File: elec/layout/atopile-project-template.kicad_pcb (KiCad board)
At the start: 2 copper layers, 40 x 40 mm, 2 parts

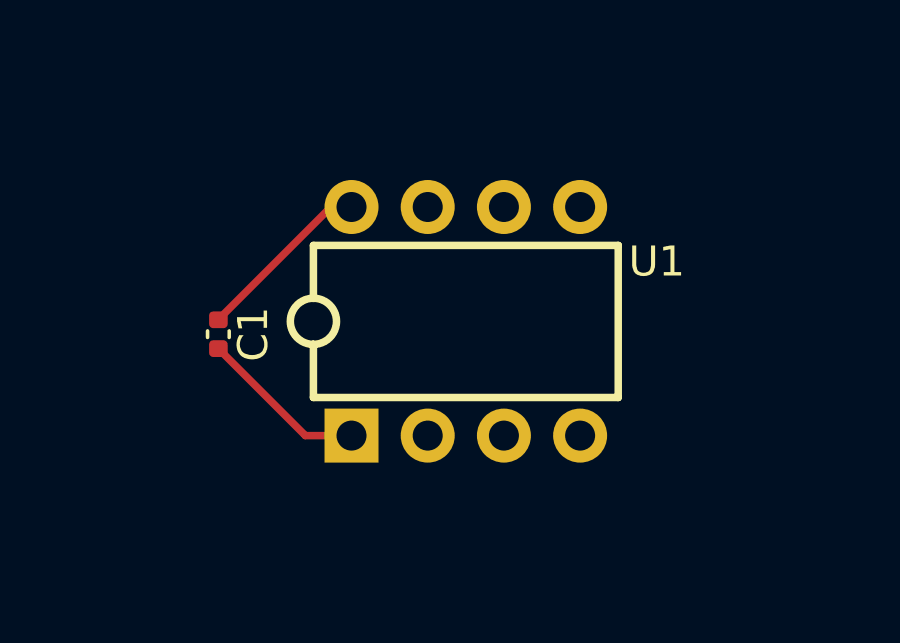
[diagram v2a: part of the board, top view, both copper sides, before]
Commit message: remove the old layout
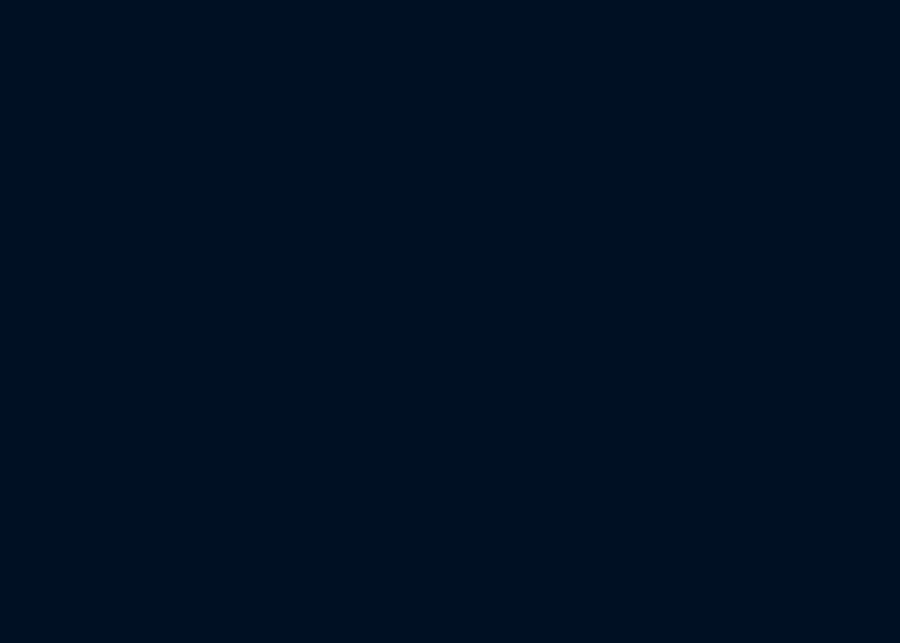
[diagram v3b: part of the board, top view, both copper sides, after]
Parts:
- removed C1: 100nF, Capacitor_SMD:C_0402_1005Metric
- removed U1: , lib:DIP-8_L9.7-W6.4-P2.54-LS7.6-BL
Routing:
- net HelloWorld-vcc_5v: track 6.00 -> 0.00 mm
- net HelloWorld-gnd: track 5.64 -> 0.00 mm
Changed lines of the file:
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@@
   )
   (net 0 "")
-  (net 1 "HelloWorld-vcc_5v")
-  (net 2 "HelloWorld-gnd")
-  (net 3 "timer-trigger")
-  (net 4 "timer-output")
-  (net 5 "timer-reset")
-  (net 6 "timer-ctrl_v")
-  (net 7 "timer-threshold")
-  (net 8 "timer-discharge")
-  (footprint "lib:DIP-8_L9.7-W6.4-P2.54-LS7.6-BL" (layer "F.Cu")
-    (at 142.24 93.98)
-    (attr smd)
-    (fp_text reference "U1" (at 6.363769 -1.989911) (layer "F.SilkS")
-        (effects (font (size 1 1) (thickness 0.15)))
-    )
-    (fp_text value "" (at 0 7.81) (layer "F.Fab")
-        (effects (font (size 1 1) (thickness 0.15)))
-    )
-    (fp_text user "${REFERENCE}" (at 0 0) (layer "F.Fab")
-        (effects (font (size 1 1) (thickness 0.15)))
-    )
-    (fp_line (start -5.08 -2.53) (end 5.08 -2.53)
-      (stroke (width 0.25) (type solid)) (layer "F.SilkS"))
-    (fp_line (start -5.08 -0.76) (end -5.08 -2.53)
-      (stroke (width 0.25) (type solid)) (layer "F.SilkS"))
-    (fp_line (start -5.08 2.54) (end -5.08 0.77)
-      (stroke (width 0.25) (type solid)) (layer "F.SilkS"))
-    (fp_line (start -5.08 2.54) (end 5.08 2.54)
-      (stroke (width 0.25) (type solid)) (layer "F.SilkS"))
-    (fp_line (start 5.08 2.54) (end 5.08 -2.53)
-      (stroke (width 0.25) (type solid)) (layer "F.SilkS"))
-    (fp_arc (start -5.093438 0.769883) (mid -5.073311 -0.769971) (end -5.08 0.77)
-      (stroke (width 0.25) (type solid)) (layer "F.SilkS"))
-    (fp_circle (center -3.94 4.45) (end -3.64 4.45)
-      (stroke (width 0.6) (type solid)) (fill none) (layer "Cmts.User"))
-    (fp_circle (center -4.83 3.94) (end -4.8 3.94)
-      (stroke (width 0.06) (type solid)) (fill none) (layer "F.Fab"))
-    (pad "1" thru_hole rect (at -3.81 3.81) (size 1.8 1.8) (drill 0.999998) (layers "*.Cu" "*.Mask")
-      (net 2 "HelloWorld-gnd"))
-    (pad "2" thru_hole circle (at -1.27 3.81) (size 1.8 1.8) (drill 0.999998) (layers "*.Cu" "*.Mask")
-      (net 3 "timer-trigger"))
-    (pad "3" thru_hole circle (at 1.27 3.81) (size 1.8 1.8) (drill 0.999998) (layers "*.Cu" "*.Mask")
-      (net 4 "timer-output"))
-    (pad "4" thru_hole circle (at 3.81 3.81) (size 1.8 1.8) (drill 0.999998) (layers "*.Cu" "*.Mask")
-      (net 5 "timer-reset"))
-    (pad "5" thru_hole circle (at 3.81 -3.81) (size 1.8 1.8) (drill 0.999998) (layers "*.Cu" "*.Mask")
-      (net 6 "timer-ctrl_v"))
-    (pad "6" thru_hole circle (at 1.27 -3.81) (size 1.8 1.8) (drill 0.999998) (layers "*.Cu" "*.Mask")
-      (net 7 "timer-threshold"))
-    (pad "7" thru_hole circle (at -1.27 -3.81) (size 1.8 1.8) (drill 0.999998) (layers "*.Cu" "*.Mask")
-      (net 8 "timer-discharge"))
-    (pad "8" thru_hole circle (at -3.81 -3.81) (size 1.8 1.8) (drill 0.999998) (layers "*.Cu" "*.Mask")
-      (net 1 "HelloWorld-vcc_5v"))
-    (model "./lib/lib.3dshapes/DIP-8_L9.8-W6.6-H3.5-LS7.62-P2.54.wrl"
-      (offset (xyz 0 -0 3))
-      (scale (xyz 1 1 1))
-      (rotate (xyz 0 0 0))
-    )
-  )
-  (footprint "Capacitor_SMD:C_0402_1005Metric" (layer "F.Cu")
-    (at 133.991711 94.410054 -90)
-    (descr "Capacitor SMD 0402 (1005 Metric), square (rectangular) end terminal, IPC_7351 nominal, (Body size source: IPC-SM-782 page 76, https://www.pcb-3d.com/wordpress/wp-content/uploads/ipc-sm-782a_amendment_1_and_2.pdf), generated with kicad-footprint-generator")
-    (tags "capacitor")
-    (attr smd)
-    (fp_text reference "C1" (at 0 -1.16 90) (layer "F.SilkS")
-        (effects (font (size 1 1) (thickness 0.15)))
-    )
-    (fp_text value "100nF" (at 0 1.16 90) (layer "F.Fab")
-        (effects (font (size 1 1) (thickness 0.15)))
-    )
-    (fp_text user "${REFERENCE}" (at 0 0 90) (layer "F.Fab")
-        (effects (font (size 0.25 0.25) (thickness 0.04)))
-    )
-    (fp_line (start -0.107836 -0.36) (end 0.107836 -0.36)
-      (stroke (width 0.12) (type solid)) (layer "F.SilkS"))
-    (fp_line (start -0.107836 0.36) (end 0.107836 0.36)
-      (stroke (width 0.12) (type solid)) (layer "F.SilkS"))
-    (fp_line (start -0.91 -0.46) (end 0.91 -0.46)
-      (stroke (width 0.05) (type solid)) (layer "F.CrtYd"))
-    (fp_line (start -0.91 0.46) (end -0.91 -0.46)
-      (stroke (width 0.05) (type solid)) (layer "F.CrtYd"))
-    (fp_line (start 0.91 -0.46) (end 0.91 0.46)
-      (stroke (width 0.05) (type solid)) (layer "F.CrtYd"))
-    (fp_line (start 0.91 0.46) (end -0.91 0.46)
-      (stroke (width 0.05) (type solid)) (layer "F.CrtYd"))
-    (fp_line (start -0.5 -0.25) (end 0.5 -0.25)
-      (stroke (width 0.1) (type solid)) (layer "F.Fab"))
-    (fp_line (start -0.5 0.25) (end -0.5 -0.25)
-      (stroke (width 0.1) (type solid)) (layer "F.Fab"))
-    (fp_line (start 0.5 -0.25) (end 0.5 0.25)
-      (stroke (width 0.1) (type solid)) (layer "F.Fab"))
-    (fp_line (start 0.5 0.25) (end -0.5 0.25)
-      (stroke (width 0.1) (type solid)) (layer "F.Fab"))
-    (pad "1" smd roundrect (at -0.48 0 270) (size 0.56 0.62) (layers "F.Cu" "F.Paste" "F.Mask") (roundrect_rratio 0.25)
-      (net 1 "HelloWorld-vcc_5v"))
-    (pad "2" smd roundrect (at 0.48 0 270) (size 0.56 0.62) (layers "F.Cu" "F.Paste" "F.Mask") (roundrect_rratio 0.25)
-      (net 2 "HelloWorld-gnd"))
-    (model "${KICAD6_3DMODEL_DIR}/Capacitor_SMD.3dshapes/C_0402_1005Metric.wrl"
-      (offset (xyz 0 0 0))
-      (scale (xyz 1 1 1))
-      (rotate (xyz 0 0 0))
-    )
-  )
   (gr_line (start 123.2 113.4) (end 123.2 80.4)
     (stroke (width 0.2) (type solid)) (layer "Edge.Cuts"))
@@
     (effects (font (size 2 2) (thickness 0.1)) (justify left bottom))
   )
-  (segment (start 137.744156 90.17) (end 133.991711 93.922445) (width 0.25) (layer "F.Cu") (net 1))
-  (segment (start 133.991711 93.922445) (end 133.991711 93.930054) (width 0.25) (layer "F.Cu") (net 1))
-  (segment (start 138.43 90.17) (end 137.744156 90.17) (width 0.25) (layer "F.Cu") (net 1))
-  (segment (start 136.891657 97.79) (end 133.991711 94.890054) (width 0.25) (layer "F.Cu") (net 2))
-  (segment (start 138.43 97.79) (end 136.891657 97.79) (width 0.25) (layer "F.Cu") (net 2))
   (group "" (id 4e3ea3a3-d408-4ad8-873b-ebd87bd265e7)
     (members
